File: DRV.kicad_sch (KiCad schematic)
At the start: 31 parts

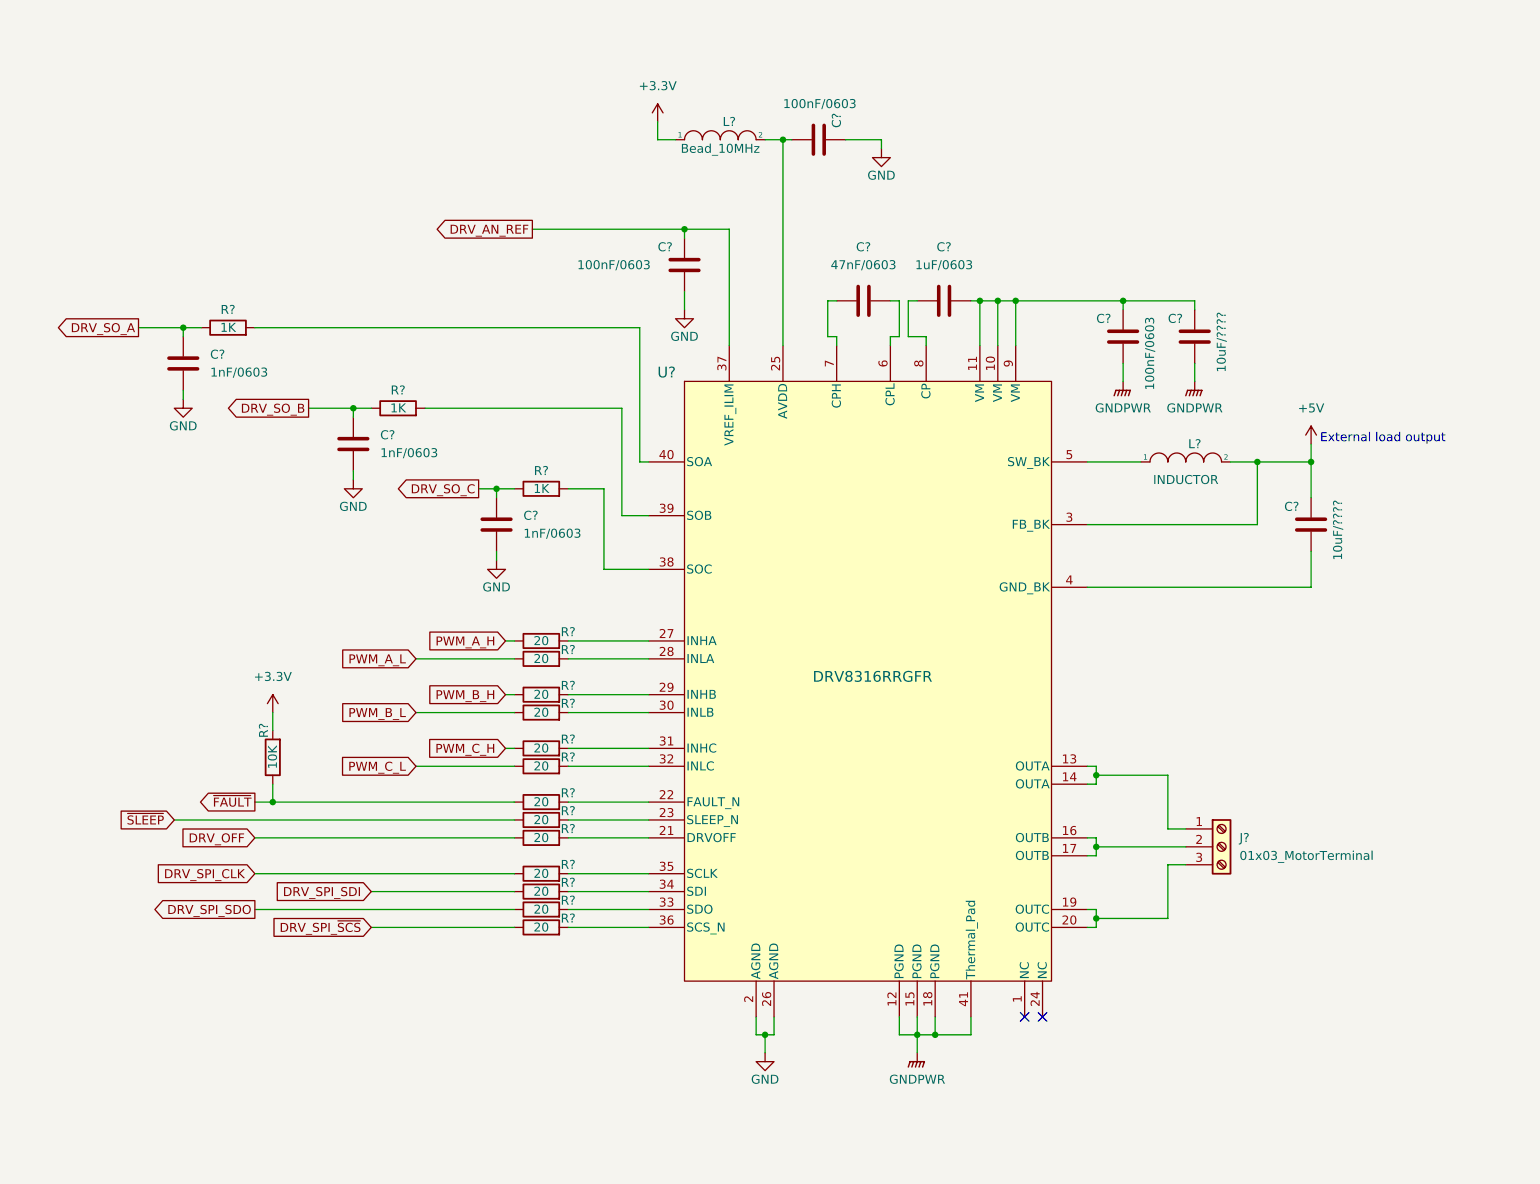
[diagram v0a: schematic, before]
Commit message: add IO, MCU, power sheets
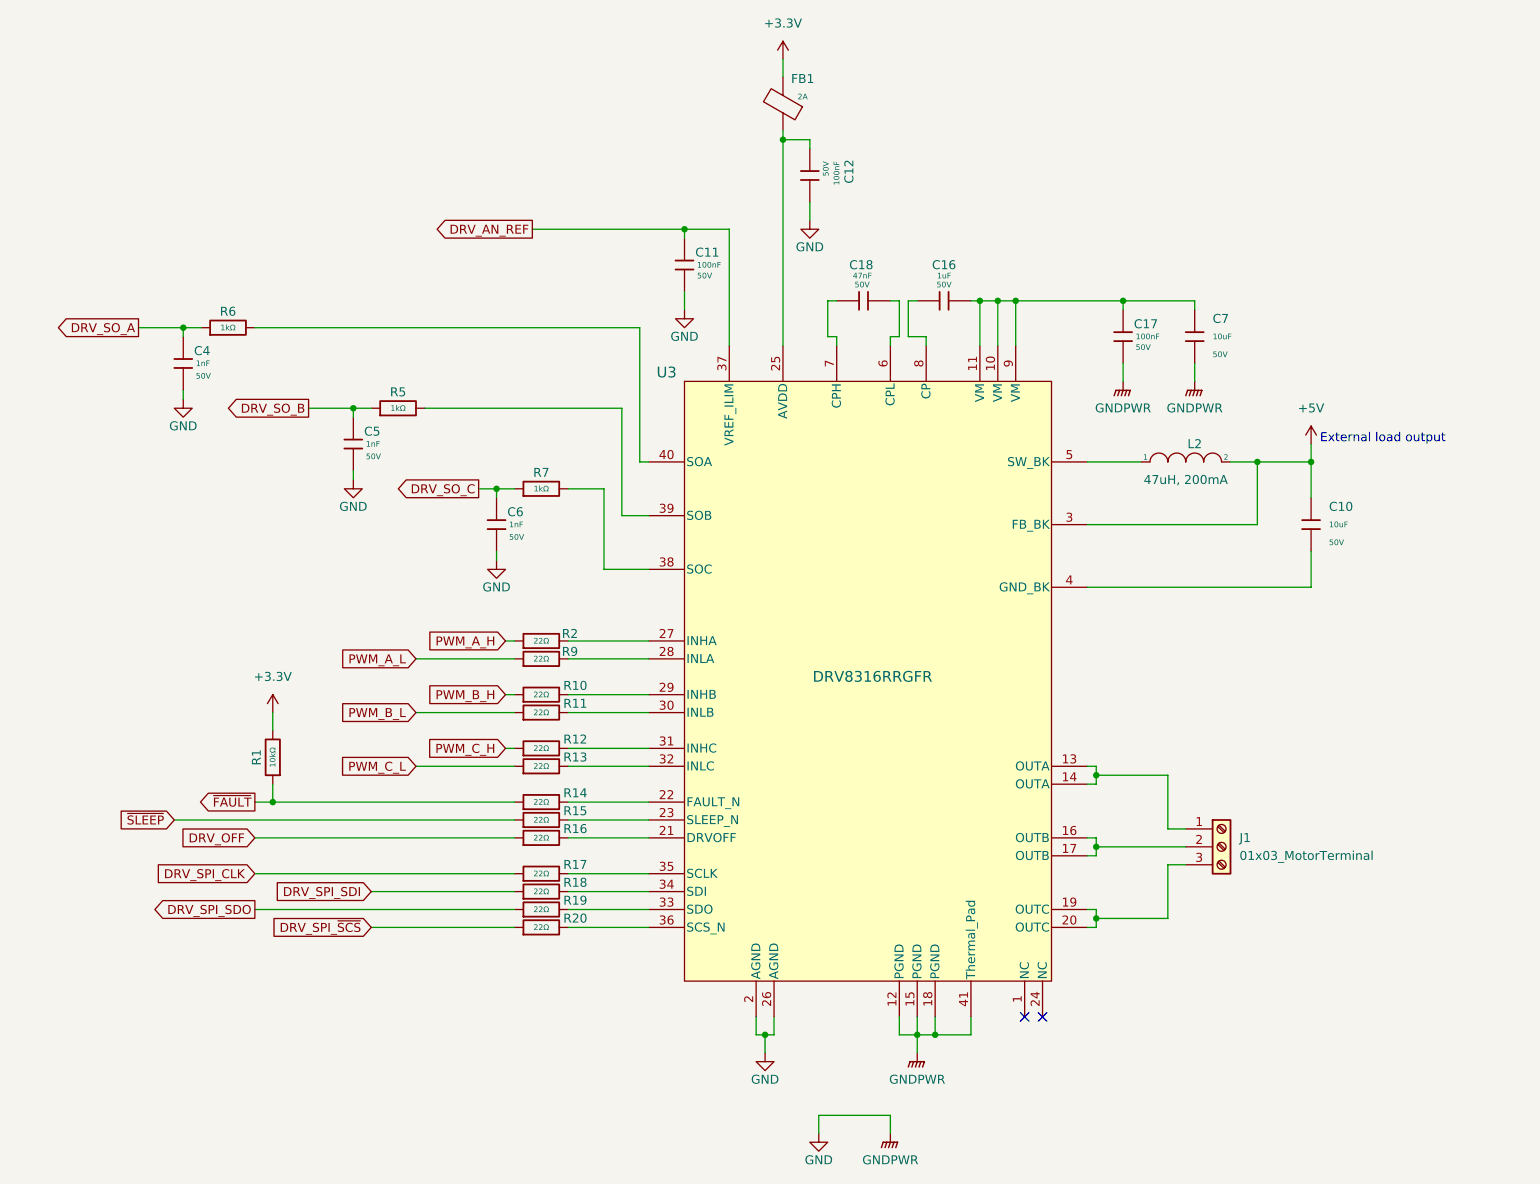
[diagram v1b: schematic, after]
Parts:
- removed C? (x3): 1nF/0603, Capacitor_SMD:C_0603_1608Metric, symbol Device:C
- removed C?: 47nF/0603, Capacitor_SMD:C_0603_1608Metric, symbol Device:C
- removed C? (x2): 10uF/????, Capacitor_SMD:C_0603_1608Metric, symbol Device:C
- removed C? (x3): 100nF/0603, Capacitor_SMD:C_0603_1608Metric, symbol Device:C
- removed C?: 1uF/0603, Capacitor_SMD:C_0603_1608Metric, symbol Device:C
- removed L?: Bead_10MHz, Inductor_SMD:L_0603_1608Metric, symbol pspice:INDUCTOR
- removed R? (x13): 20, Resistor_SMD:R_0603_1608Metric, symbol Device:R
- removed R? (x3): 1K, Resistor_SMD:R_0603_1608Metric, symbol Device:R
- removed R?: 10K, Resistor_SMD:R_0603_1608Metric, symbol Device:R
- added C10, C7: 10uF, PCM_JLCPCB:C_1206, symbol PCM_JLCPCB-Capacitors:1206,10uF
- added C11, C12, C17: 100nF, PCM_JLCPCB:C_0603, symbol PCM_JLCPCB-Capacitors:0603,100nF
- added C16: 1uF, PCM_JLCPCB:C_0603, symbol PCM_JLCPCB-Capacitors:0603,1uF
- added C18: 47nF, PCM_JLCPCB:C_0603, symbol PCM_JLCPCB-Capacitors:0603,47nF
- added C4, C5, C6: 1nF, PCM_JLCPCB:C_0603, symbol PCM_JLCPCB-Capacitors:0603,1nF
- added FB1: ~, PCM_JLCPCB:FB_0603, symbol PCM_JLCPCB-Inductors:Ferrite,0603,(2)
- added R1: 10kΩ, PCM_JLCPCB:R_0603, symbol PCM_JLCPCB-Resistors:0603,10kΩ
- added R10, R11, R12, R13, R14, R15, R16, R17, R18, R19, R2, R20, R9: 22Ω, PCM_JLCPCB:R_0603, symbol PCM_JLCPCB-Resistors:0603,22Ω
- added R5, R6, R7: 1kΩ, PCM_JLCPCB:R_0603, symbol PCM_JLCPCB-Resistors:0603,1kΩ
- L2: renamed from L?; value INDUCTOR -> 47uH, 200mA
- gave numbers to parts that had none: 2
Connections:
- net GNDPWR is gone; now on net GND: U3.12 (PGND), U3.15 (PGND), U3.18 (PGND), U3.41 (Thermal_Pad)
- net +3.3V: now also FB1.2, R1.2
- net +5V: now also C10.1
- net DRV_AN_REF: now also C11.1
- net DRV_OFF: now also R16.1
- net DRV_SO_A: now also C4.1, R6.1
- net DRV_SO_B: now also C5.1, R5.1
- net DRV_SO_C: now also C6.1, R7.1
- net DRV_SPI_CLK: now also R17.1
- net DRV_SPI_SDI: now also R18.1
- net DRV_SPI_SDO: now also R19.1
- net DRV_SPI_~{SCS}: now also R20.1
- net GND: now also C11.2, C12.2, C17.2, C4.2, C5.2, C6.2, C7.2
- net PWM_A_H: now also R2.1
- net PWM_A_L: now also R9.1
- net PWM_B_H: now also R10.1
- net PWM_B_L: now also R11.1
- net PWM_C_H: now also R12.1
- net PWM_C_L: now also R13.1
- net ~{FAULT}: now also R1.1, R14.1
- net ~{SLEEP}: now also R15.1
- net at U3.27 (INHA): now also R2.2
- net at U3.29 (INHB): now also R10.2
- net at U3.21 (DRVOFF): now also R16.2
- net at U3.38 (SOC): now also R7.2
- net at U3.31 (INHC): now also R12.2
- net at U3.28 (INLA): now also R9.2
- net at U3.7 (CPH): now also C18.1
- net at U3.6 (CPL): now also C18.2
- net at U3.36 (SCS_N): now also R20.2
- net at U3.4 (GND_BK): now also C10.2
- net at U3.22 (FAULT_N): now also R14.2
- net at U3.10 (VM), U3.11 (VM), U3.9 (VM): now also C16.2, C17.1, C7.1
- net at U3.23 (SLEEP_N): now also R15.2
- net at U3.25 (AVDD): now also C12.1, FB1.1
- net at U3.30 (INLB): now also R11.2
- net at U3.32 (INLC): now also R13.2
- net at U3.33 (SDO): now also R19.2
- net at U3.34 (SDI): now also R18.2
- net at U3.35 (SCLK): now also R17.2
- net at U3.39 (SOB): now also R5.2
- net at U3.40 (SOA): now also R6.2
- net at U3.8 (CP): now also C16.1

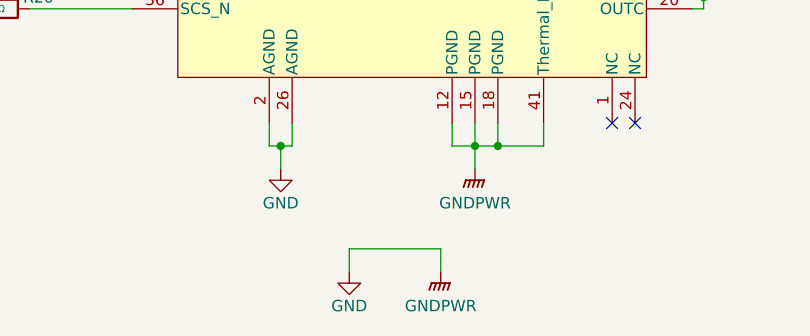
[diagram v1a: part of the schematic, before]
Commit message: Add encoder sheet
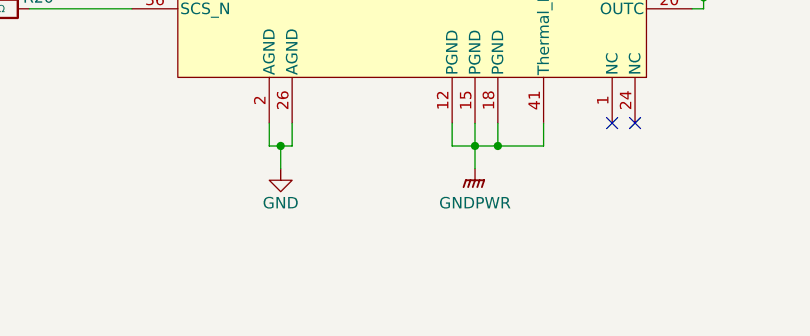
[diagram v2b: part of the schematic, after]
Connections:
- net GND: no longer C17.2, C7.2, U3.12 (PGND), U3.15 (PGND), U3.18 (PGND), U3.41 (Thermal_Pad)
- new net GNDPWR: C17.2, C7.2, U3.12 (PGND), U3.15 (PGND), U3.18 (PGND), U3.41 (Thermal_Pad)

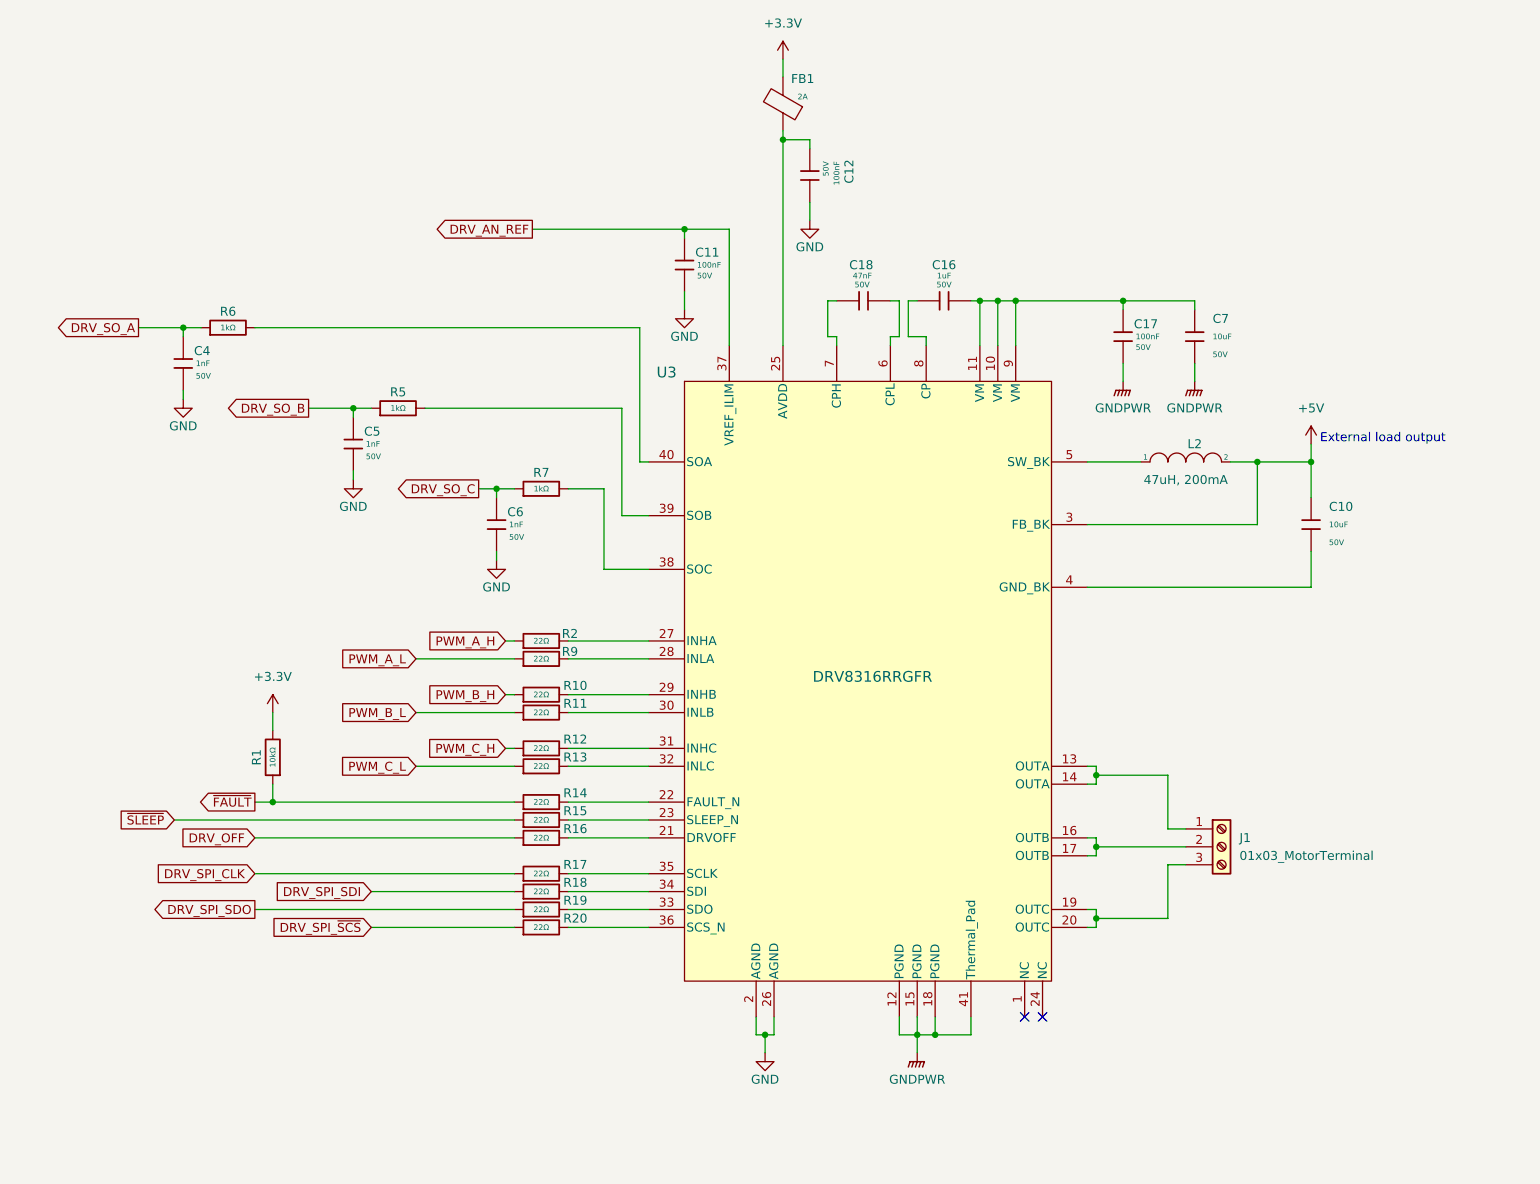
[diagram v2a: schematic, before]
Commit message: Add buck converter, add part of pinmap to mcu
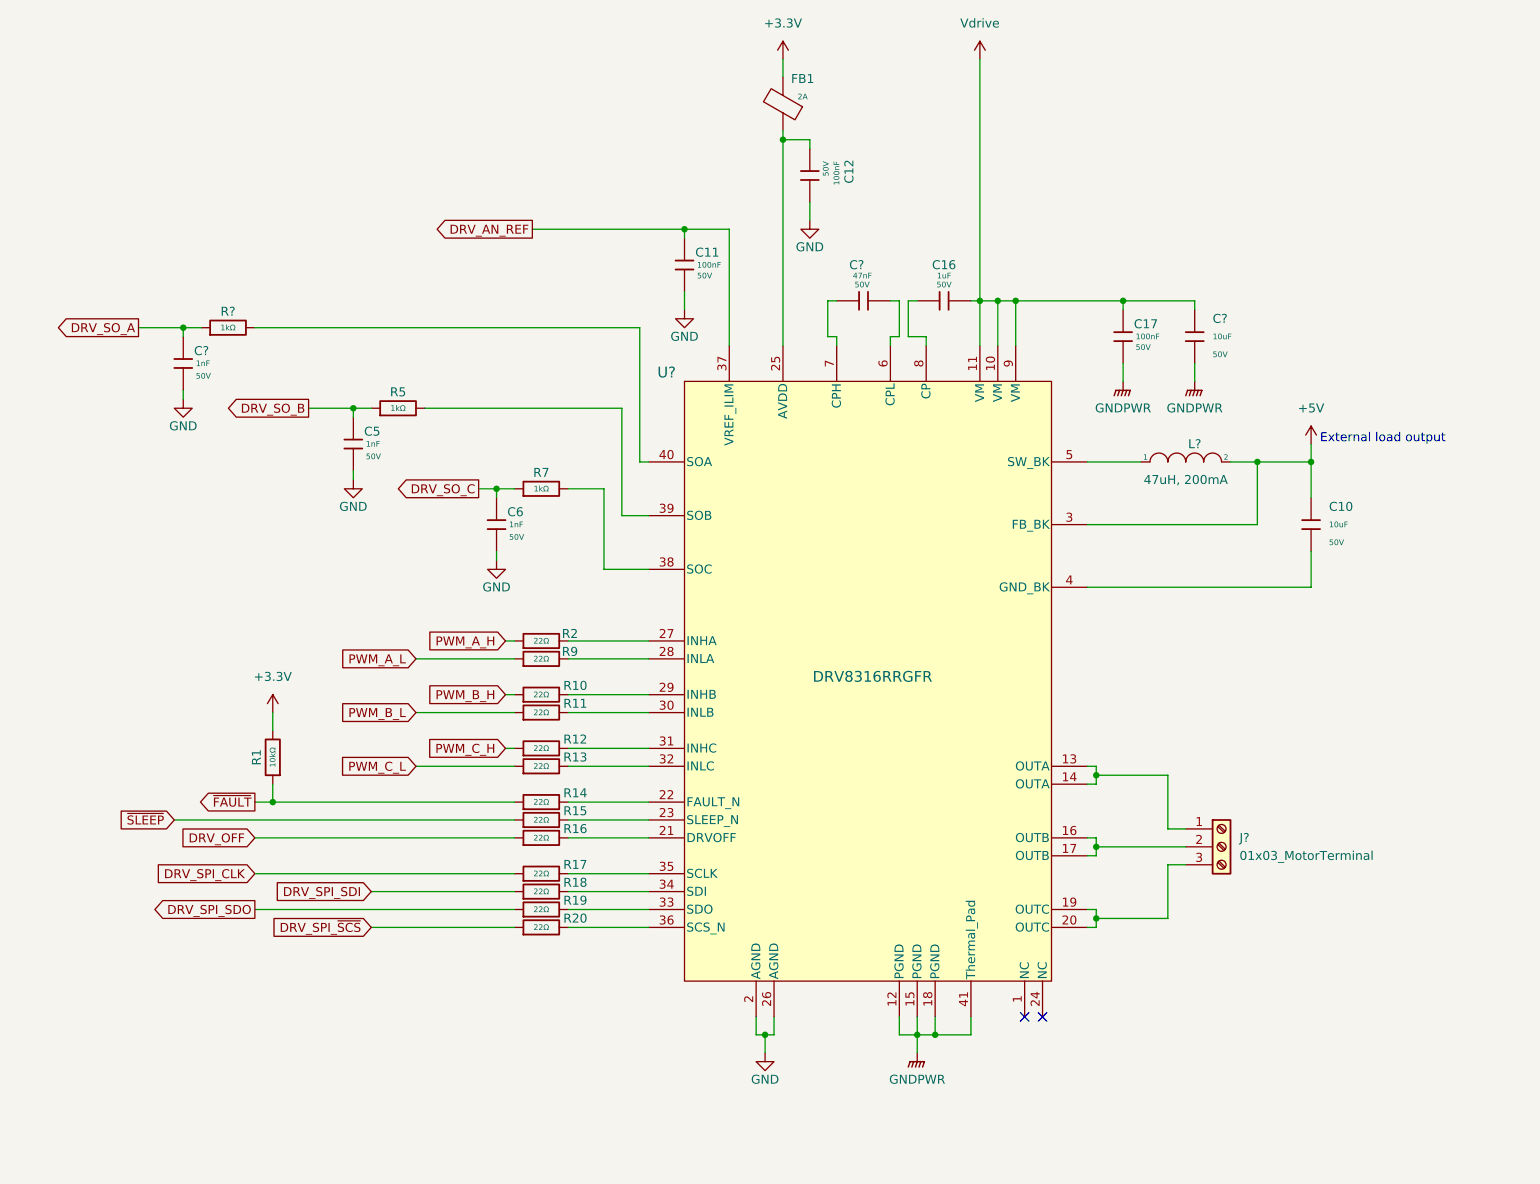
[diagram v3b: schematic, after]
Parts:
- renumbered C4 to C?, C18 to C?, C7 to C?, J1 to J?, L2 to L?, R6 to R?, U3 to U?
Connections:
- net Vdrive: now reaches C16.2, C17.1, C?.1, U?.10 (VM), U?.11 (VM), U?.9 (VM)
